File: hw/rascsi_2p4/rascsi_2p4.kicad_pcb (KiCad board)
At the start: 2 copper layers, 65 x 56 mm, 72 parts, among them J1 Raspberry_Pi_2_3, J10 Conn_01x04_Male, J2 DNP, J20 171826-4, J3 Conn_02x25_Odd_Even, J4 I2C Pinout, J5 DNP, J6 CONNFLY DB-25, J7 DNP, J8 USB_B_Micro, J9 Conn_02x25_Odd_Even, U1 SN74LS641-1DW, U2 SN74LS641-1DW, U3 SN74LS641-1DW, U4 SN74LS641-1DW, U5 UCC5606PWPTR, U6 UCC5606PWPTR, X1 Mac, X3 Mac, X7 Pi, X8 Pi

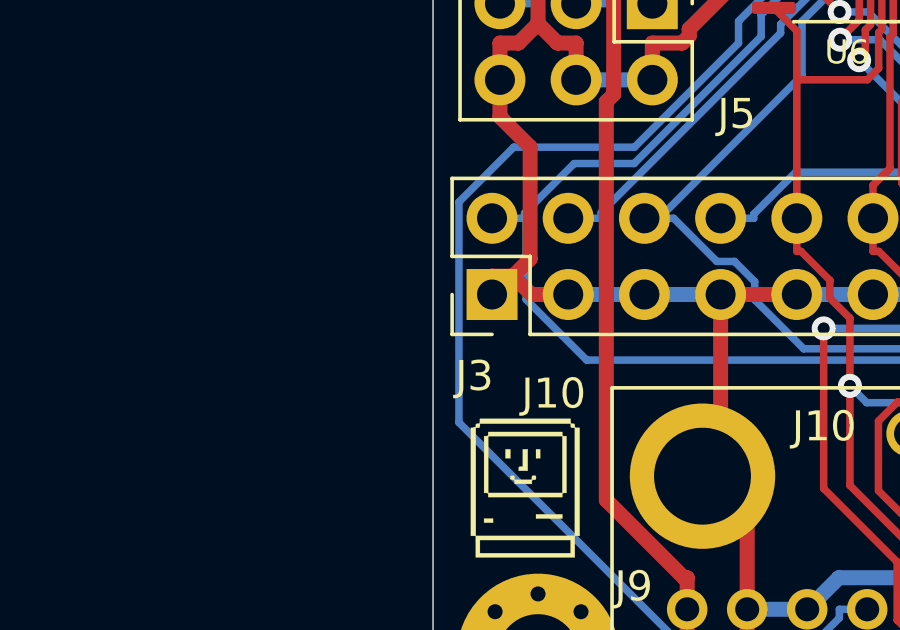
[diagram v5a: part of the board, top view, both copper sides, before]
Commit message: fixed part positioning at JLCPCB by removing 2x25 Pin Header from Handmount
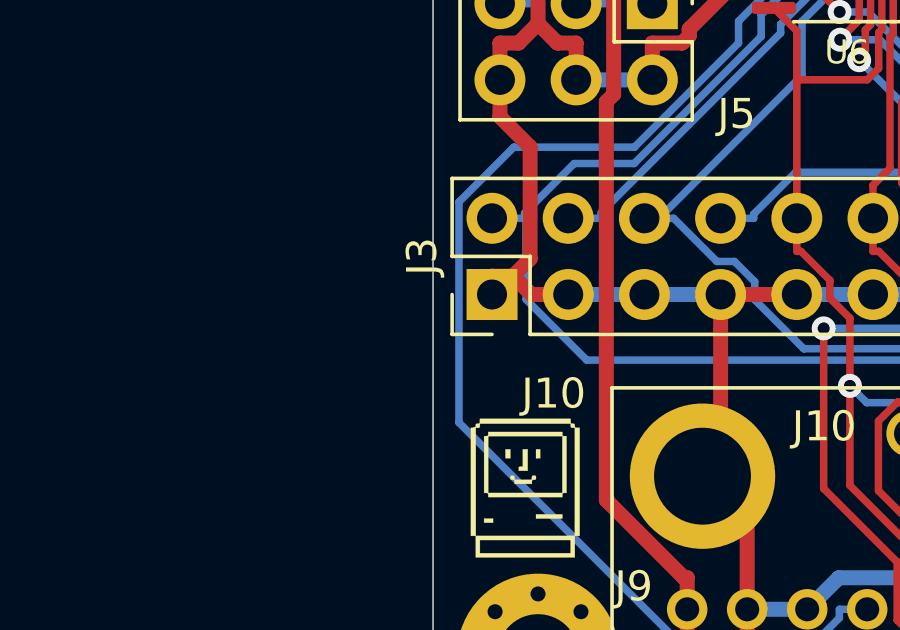
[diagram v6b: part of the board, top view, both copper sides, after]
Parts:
- J3: footprint amiga:PinHeader_2x25_P2.54mm_Vertical_JLCPCB_hand_mount -> Connector_PinHeader_2.54mm:PinHeader_2x25_P2.54mm_Vertical

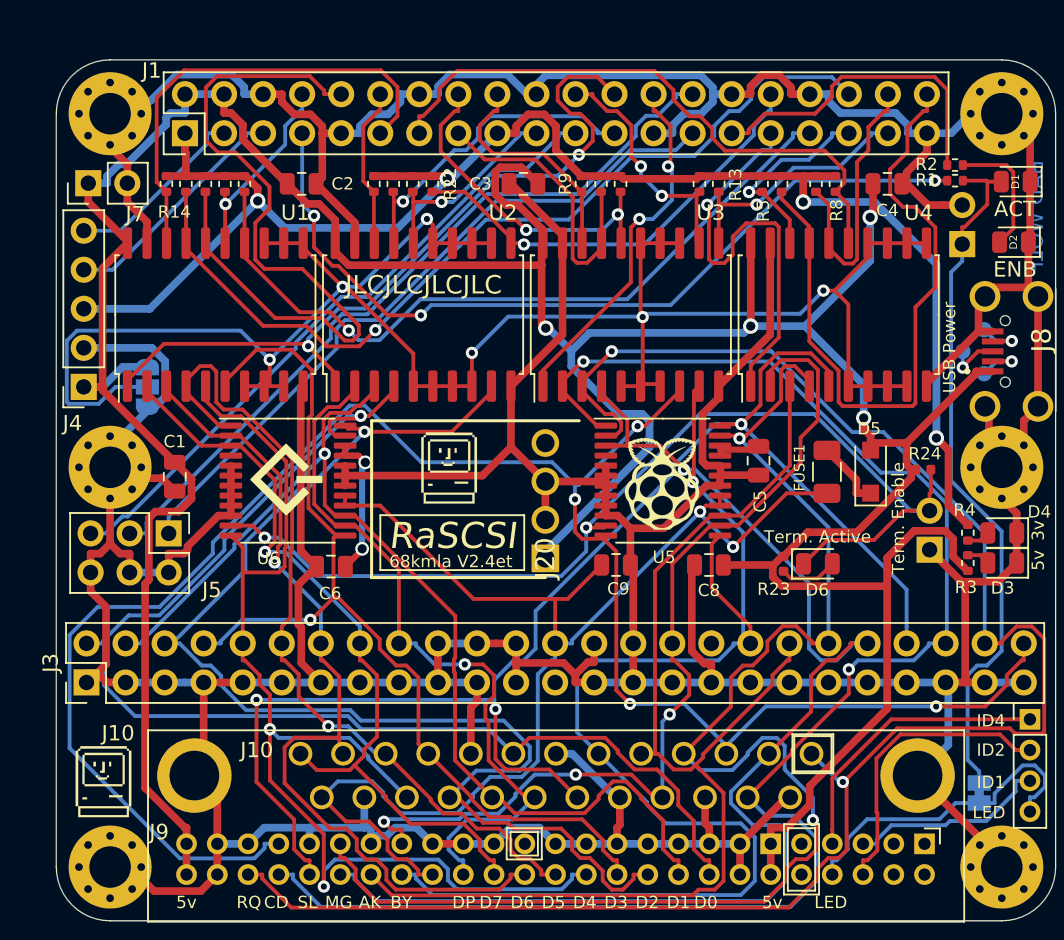
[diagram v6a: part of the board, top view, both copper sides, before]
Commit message: changed /TERM_ENABLE to TERM_ENABLE so that a plugged jumper enables termination
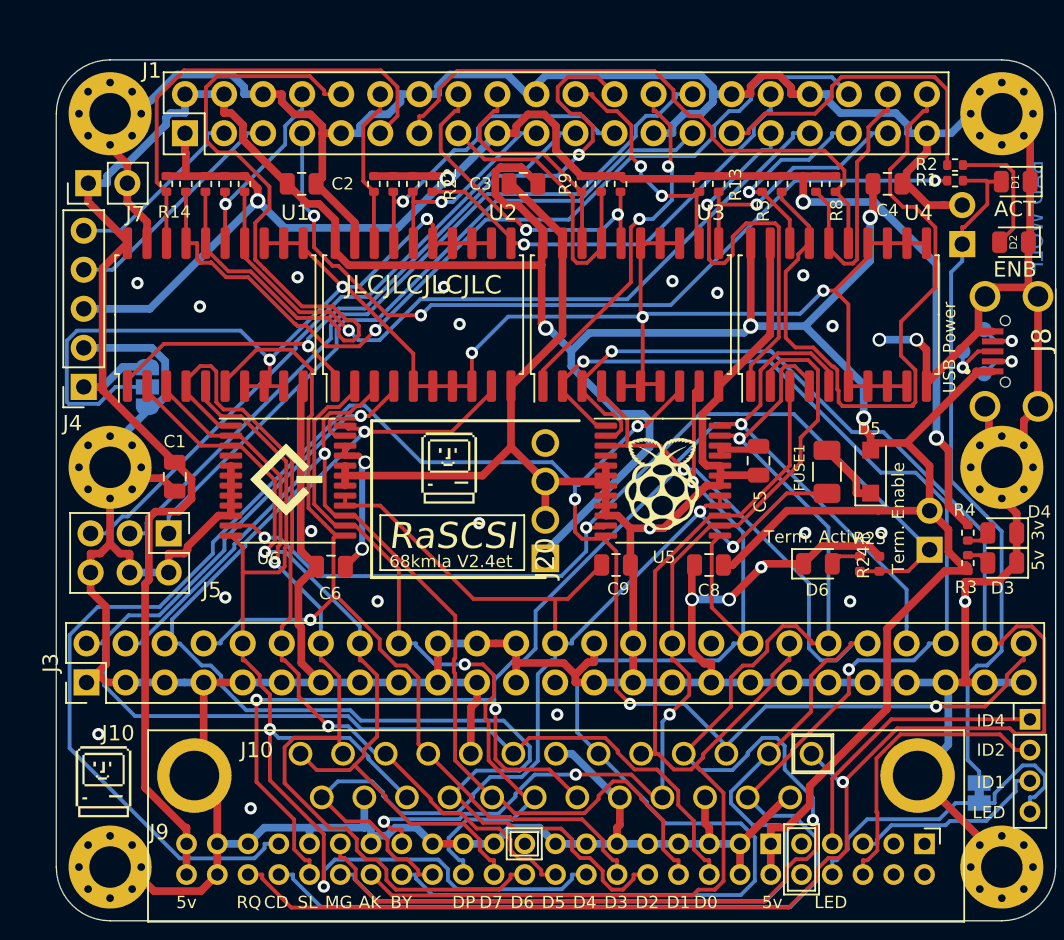
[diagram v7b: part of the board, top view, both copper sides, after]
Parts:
- moved R24 6.76 mm to (58.0, 35.3), turned to 270 degrees
- moved R23 4.97 mm to (56.8, 35.3), turned to 90 degrees
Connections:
- D6 pad 1: ~TERM_ENABLE -> GND
- JP2 pad 1: GND -> TERM_ENABLE
- JP2 pad 2: ~TERM_ENABLE -> +5V
- R23 pad 1: +5V -> TERM_ENABLE
- R24 pad 1: ~TERM_ENABLE -> GND
- R24 pad 2: +5V -> TERM_ENABLE
- U5 pad 11: ~TERM_ENABLE -> TERM_ENABLE
- U6 pad 11: ~TERM_ENABLE -> TERM_ENABLE
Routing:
- net ~TERM_ENABLE: track 68.3 -> 0.00 mm, vias 2 -> 0
- net TERM_ENABLE: track 0.00 -> 62.9 mm, vias 0 -> 2
- net GND: track 552.9 -> 569.3 mm, vias 0 -> 26
- net +5V: track 245.5 -> 239.3 mm
- net PI-ACK: track 43.8 -> 46.6 mm
- net Net-(D6-Pad2): track 3.76 -> 1.99 mm
